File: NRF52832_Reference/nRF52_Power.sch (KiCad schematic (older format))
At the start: 37 parts

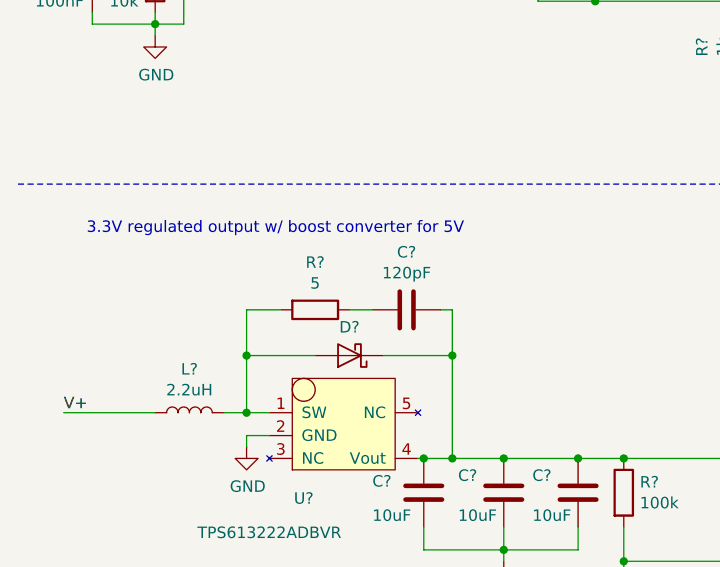
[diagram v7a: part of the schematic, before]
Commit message: Finished boost converter and regulators footprint assignments.
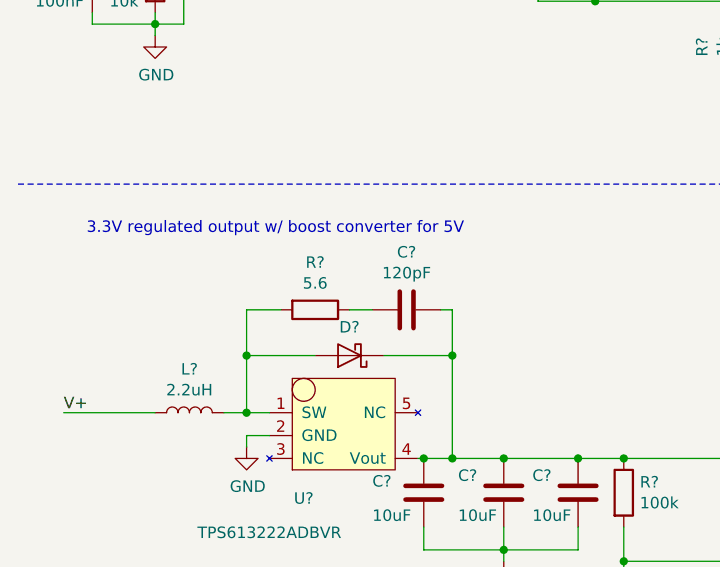
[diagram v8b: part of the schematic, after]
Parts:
- D?: footprint (none) -> Diode_SMD:D_SOD-123F
- L?: footprint (none) -> Custom_Footprints:L_1008_2520Metric
- R?: value 5 -> 5.6
- U?: footprint (none) -> Package_TO_SOT_SMD:SOT-23-5_HandSoldering
- U?: footprint (none) -> Package_TO_SOT_SMD:SOT-353_SC-70-5_Handsoldering
- U?: footprint (none) -> Package_TO_SOT_SMD:SOT-223-3_TabPin2
- U?: footprint (none) -> Package_TO_SOT_SMD:SOT-23
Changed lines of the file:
@@
 F 0 "U?" H 1750 4725 50  0000 C CNN
 F 1 "TPS613222ADBVR" H 1600 4575 50  0000 C CNN
-F 2 "" H 1850 5450 50  0001 C CNN
+F 2 "Package_TO_SOT_SMD:SOT-23-5_HandSoldering" H 1850 5450 50  0001 C CNN
 F 3 "" H 1850 5450 50  0001 C CNN
 	1    1850 5000
@@
 F 0 "L?" V 1440 4900 50  0000 C CNN
 F 1 "2.2uH" V 1349 4900 50  0000 C CNN
-F 2 "" H 1250 4900 50  0001 C CNN
+F 2 "Custom_Footprints:L_1008_2520Metric" H 1250 4900 50  0001 C CNN
 F 3 "~" H 1250 4900 50  0001 C CNN
 	1    1250 4900
@@
 F 0 "D?" H 1950 4526 50  0000 C CNN
 F 1 "D_Schottky" H 1950 4525 50  0001 C CNN
-F 2 "" H 1950 4650 50  0001 C CNN
+F 2 "Diode_SMD:D_SOD-123F" H 1950 4650 50  0001 C CNN
 F 3 "~" H 1950 4650 50  0001 C CNN
 	1    1950 4650
@@
 AR Path="/5BF31556/5BF591C6" Ref="R?"  Part="1"
 F 0 "R?" V 1593 4450 50  0000 C CNN
-F 1 "5" V 1684 4450 50  0000 C CNN
+F 1 "5.6" V 1684 4450 50  0000 C CNN
 F 2 "Resistor_SMD:R_0603_1608Metric_Pad1.05x0.95mm_HandSolder" V 1730 4450 50  0001 C CNN
 F 3 "~" H 1800 4450 50  0001 C CNN
@@
 F 0 "U?" H 4000 6015 50  0000 C CNN
 F 1 "LMV331ICT" H 4000 5924 50  0000 C CNN
-F 2 "" H 3925 5950 50  0001 C CNN
+F 2 "Package_TO_SOT_SMD:SOT-353_SC-70-5_Handsoldering" H 3925 5950 50  0001 C CNN
 F 3 "" H 3925 5950 50  0001 C CNN
 	1    3975 5650
@@
 F 0 "U?" H 1925 7290 50  0000 C CNN
 F 1 "AP2114HA-3.3TRG1" H 1925 7199 50  0000 C CNN
-F 2 "" H 1925 7225 50  0001 C CNN
+F 2 "Package_TO_SOT_SMD:SOT-223-3_TabPin2" H 1925 7225 50  0001 C CNN
 F 3 "" H 1925 7225 50  0001 C CNN
 	1    1925 6975
@@
 F 0 "U?" H 4025 7165 50  0000 C CNN
 F 1 "AP2138N-3.0TRG1" H 4025 7074 50  0000 C CNN
-F 2 "" H 4025 7150 50  0001 C CNN
+F 2 "Package_TO_SOT_SMD:SOT-23" H 4025 7150 50  0001 C CNN
 F 3 "" H 4025 7150 50  0001 C CNN
 	1    4025 6900
